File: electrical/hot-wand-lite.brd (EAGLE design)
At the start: 112 x 72 mm, 76 parts, among them IC1 12V R-78K12-2.0, Q1 NCHAN, Q2 SIRS5800DP-T1-GE3, Q3 DMTH64M2LPDWQ-13, Q4 2N7002K, Q5 G3404, U1 SEEED-XIAO-SAMD21, U2 1EDN8511BXUSA1, U3 LM74700QDBVTQ1, U4 AP53781

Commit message: lite part numbers
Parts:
- added R20: 470Ω, hot-wand:0603-RES
- IC2: value (none) -> AMS1117-5.0
- R17: value 79K -> 3K
- R18: value 470Ω -> 75K
- moved R18 51.9 mm to (19.0, 23.9), turned to 270 degrees
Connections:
- new net N$2: R17.2, R18.1
- net ADC: now also R20.1; no longer R18.1
- net GND: now also R20.2; no longer R18.2
- net N$9: now also R18.2; no longer R17.2
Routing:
- net N$9: track 23.9 -> 20.5 mm
- net N$2: track 0.00 -> 1.70 mm

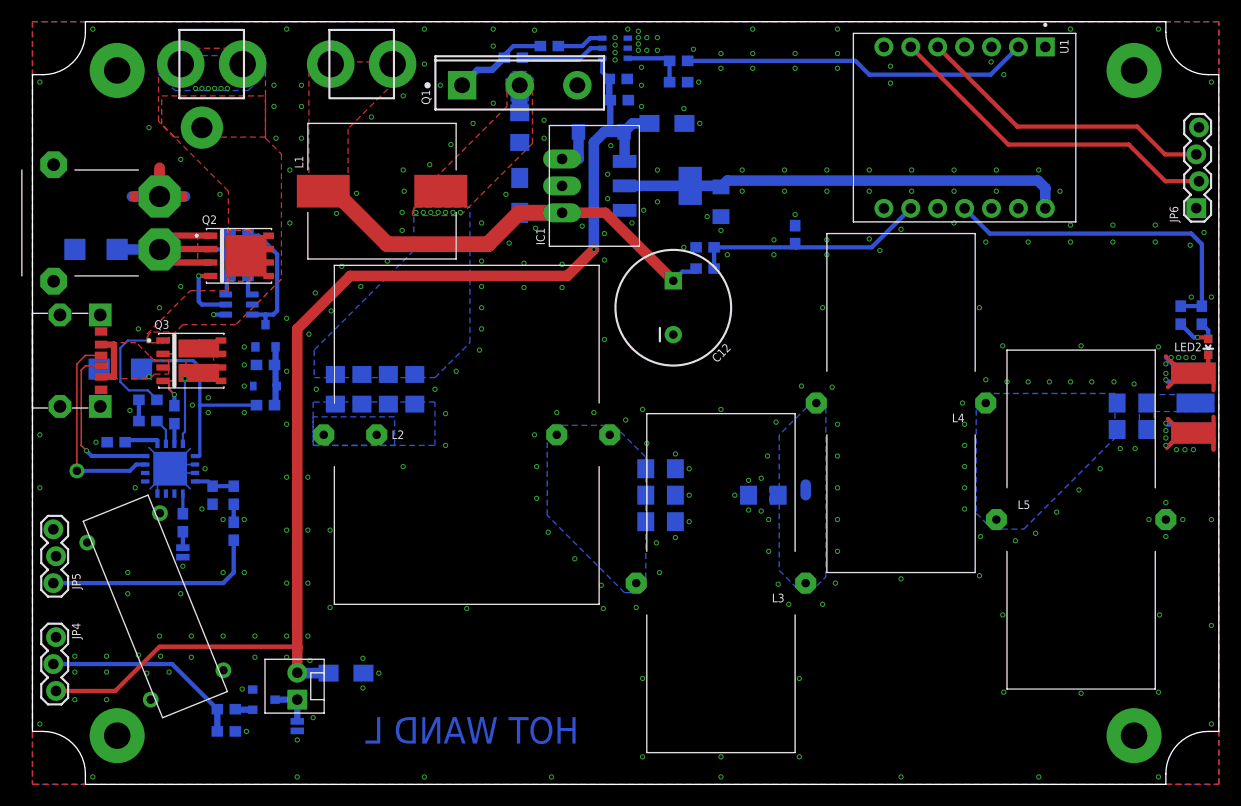
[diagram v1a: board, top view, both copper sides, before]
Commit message: routing, compatible with rp2040
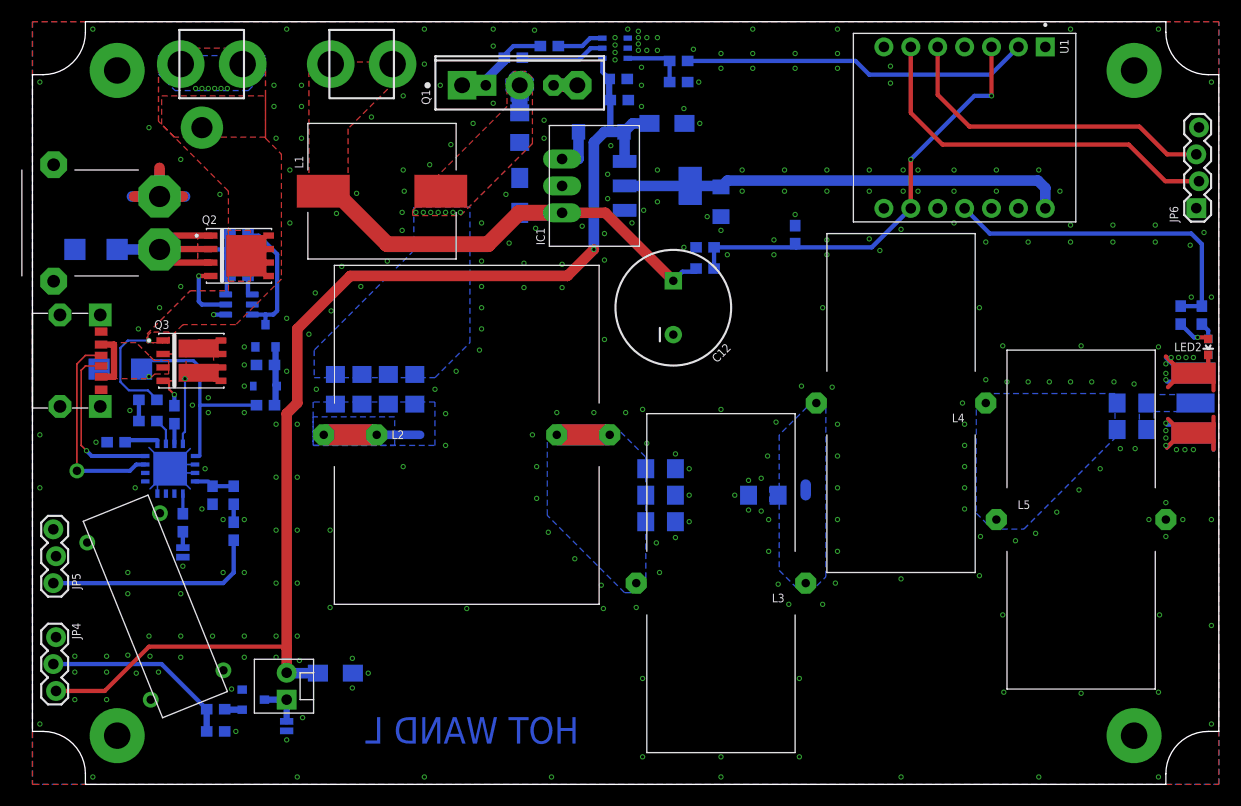
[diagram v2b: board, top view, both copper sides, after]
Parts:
- Q1: device hot-wand:INF-PG-TO247-3 -> hot-wand:TO247-COMBO
- moved C16 1.00 mm to (28.6, 10.5)
- moved FAN1 1.00 mm to (24.0, 8.00)
- moved Q5 1.00 mm to (20.8, 8.00)
- moved R7 1.00 mm to (17.3, 5.00)
- moved R8 1.00 mm to (17.3, 7.10)
- moved SJ1 1.00 mm to (24.0, 5.50)
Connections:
- net ADC: now also U1.3
- net FET-GATE: now also Q1.1B
- net GND: now also Q1.3B
- net N$3: now also L2.1C, L2.1D
- net N$4: now also L2.2C, L2.2D
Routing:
- net ADC: track 22.5 -> 41.9 mm, vias 0 -> 2
- net N$3: track 0.00 -> 11.7 mm
- net N$4: track 0.00 -> 5.10 mm
- net GND: track 47.0 -> 51.4 mm, vias 322 -> 323
- net SEL2: track 32.5 -> 36.1 mm
- net SEL3: track 28.6 -> 31.3 mm
- net SWDIO: track 19.3 -> 18.3 mm
- net +12V: track 117.9 -> 117.3 mm

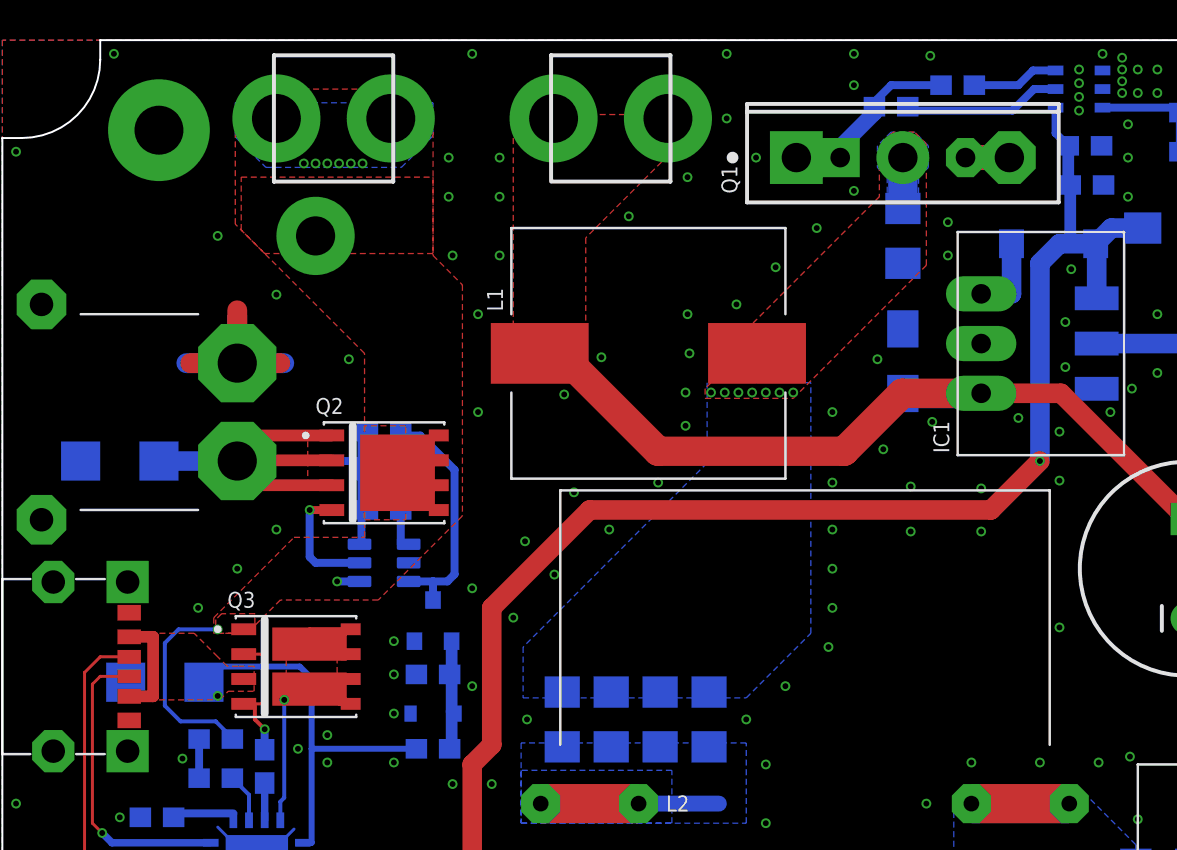
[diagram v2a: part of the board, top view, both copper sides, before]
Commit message: splash screen is now a full feature
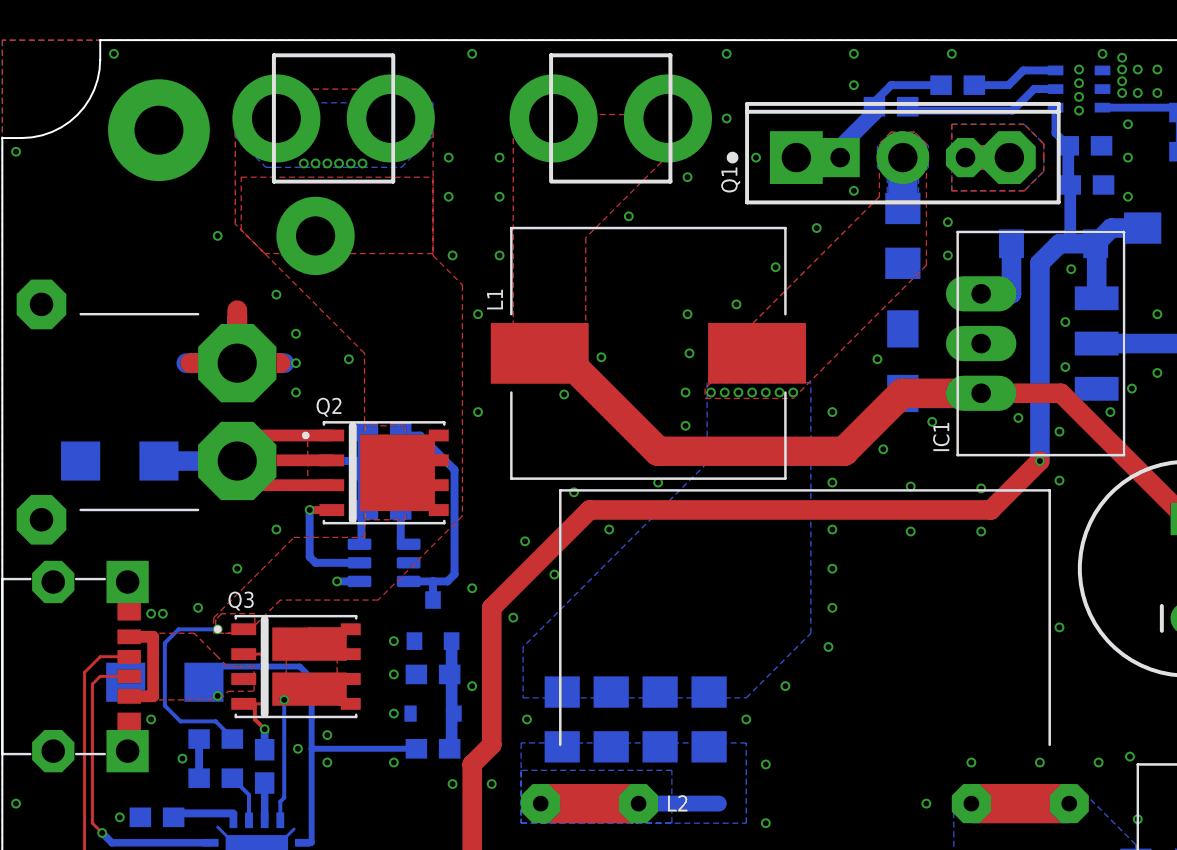
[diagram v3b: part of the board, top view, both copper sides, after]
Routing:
- net GND: vias 323 -> 329
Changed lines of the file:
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@@
 <wire x1="47.8" y1="31.5" x2="47.8" y2="34.5" width="0" layer="41"/>
 <wire x1="56.1" y1="31.5" x2="56.1" y2="34.5" width="0" layer="41"/>
+<rectangle x1="12.5" y1="49" x2="15" y2="52.1" layer="29"/>
+<rectangle x1="8" y1="38.2" x2="10" y2="41.8" layer="29"/>
 </plain>
 <attributes>
@@
 </element>
 <element name="R15" library="hot-wand" package="0603-RES" value="DNP" x="14.2" y="24.7" smashed="yes" rot="MR270">
-<attribute name="NAME" x="13.338" y="25.789" size="0.8128" layer="26" font="fixed" rot="MR270"/>
-<attribute name="VALUE" x="12.343" y="25.816" size="0.8128" layer="28" font="vector" rot="MR270"/>
+<attribute name="NAME" x="12.838" y="24.689" size="0.8128" layer="26" font="fixed" rot="MR270"/>
+<attribute name="VALUE" x="11.843" y="24.716" size="0.8128" layer="28" font="vector" rot="MR270"/>
 <attribute name="JLC-DNP" value="1" x="14.2" y="24.7" size="1.778" layer="28" rot="MR270" display="off"/>
 </element>
@@
 </element>
 <element name="SJ2" library="hot-wand" package="SJ_2S-NO" value="" x="14.2" y="21.9" smashed="yes" rot="MR270">
-<attribute name="NAME" x="12.83" y="23.008" size="0.8128" layer="26" font="fixed" rot="MR270"/>
+<attribute name="NAME" x="12.83" y="22.208" size="0.8128" layer="26" font="fixed" rot="MR270"/>
 <attribute name="VALUE" x="15.851" y="22.808" size="0.4064" layer="28" rot="MR270"/>
 <attribute name="JLC-DNP" value="1" x="14.2" y="21.9" size="1.778" layer="28" rot="MR270" display="off"/>
@@
 <via x="48.3" y="61" extent="1-16" drill="0.3" shape="octagon"/>
 <via x="48.3" y="62.7" extent="1-16" drill="0.3" shape="octagon"/>
-<via x="47.4" y="71.2" extent="1-16" drill="0.3" shape="octagon"/>
+<via x="48.5" y="71.3" extent="1-16" drill="0.3" shape="octagon"/>
 <via x="43.5" y="69.7" extent="1-16" drill="0.3" shape="octagon"/>
 <via x="38.5" y="66" extent="1-16" drill="0.3" shape="octagon"/>
@@
 <wire x1="49.2" y1="66" x2="51.4" y2="66" width="1.27" layer="1"/>
 <via x="25" y="34" extent="1-16" drill="0.3" shape="octagon"/>
+<via x="7.6" y="42.7" extent="1-16" drill="0.3" shape="octagon"/>
+<via x="8.2" y="42.7" extent="1-16" drill="0.3" shape="octagon"/>
+<via x="7.6" y="37.3" extent="1-16" drill="0.3" shape="octagon"/>
+<via x="15" y="55.5" extent="1-16" drill="0.3" shape="octagon"/>
+<via x="15" y="57" extent="1-16" drill="0.3" shape="octagon"/>
+<via x="15" y="54" extent="1-16" drill="0.3" shape="octagon"/>
+<polygon width="0.2032" layer="16" spacing="0.2032" isolate="0.2032" thermals="no" rank="3">
+<vertex x="48.5" y="66"/>
+<vertex x="48.5" y="67.7"/>
+<vertex x="52.2" y="67.7"/>
+<vertex x="53.2" y="66.7"/>
+<vertex x="53.2" y="66"/>
+<vertex x="53.2" y="65.3"/>
+<vertex x="52.2" y="64.3"/>
+<vertex x="48.5" y="64.3"/>
+</polygon>
+<polygon width="0.2032" layer="1" spacing="0.2032" isolate="0.2032" thermals="no" rank="3">
+<vertex x="48.5" y="66"/>
+<vertex x="48.5" y="64.3"/>
+<vertex x="52.2" y="64.3"/>
+<vertex x="53.2" y="65.3"/>
+<vertex x="53.2" y="66"/>
+<vertex x="53.2" y="66.7"/>
+<vertex x="52.2" y="67.7"/>
+<vertex x="48.5" y="67.7"/>
+</polygon>
 </signal>
 <signal name="+24V">
@@
 <contactref element="U2" pad="3"/>
 <contactref element="R4" pad="1"/>
-<wire x1="53.8" y1="70.45" x2="52.65" y2="70.45" width="0.4064" layer="16"/>
-<wire x1="52.65" y1="70.45" x2="51.9" y2="69.7" width="0.4064" layer="16"/>
-<wire x1="51.9" y1="69.7" x2="49.65" y2="69.7" width="0.4064" layer="16"/>
+<wire x1="53.8" y1="70.45" x2="52.15" y2="70.45" width="0.4064" layer="16"/>
+<wire x1="52.15" y1="70.45" x2="51.4" y2="69.7" width="0.4064" layer="16"/>
+<wire x1="51.4" y1="69.7" x2="49.65" y2="69.7" width="0.4064" layer="16"/>
 </signal>
 <signal name="FET-GATE">
@@
 <vertex x="47.2" y="66.7"/>
 <vertex x="46.6" y="67.3"/>
-<vertex x="45.5" y="67.3"/>
-<vertex x="44.8" y="66.6"/>
+<vertex x="45.4" y="67.3"/>
+<vertex x="44.8" y="66.7"/>
 <vertex x="44.8" y="64"/>
 <vertex x="37" y="56.2"/>
